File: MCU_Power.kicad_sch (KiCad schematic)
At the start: 36 parts, among them U3 SPC5676RDK3MVU1R

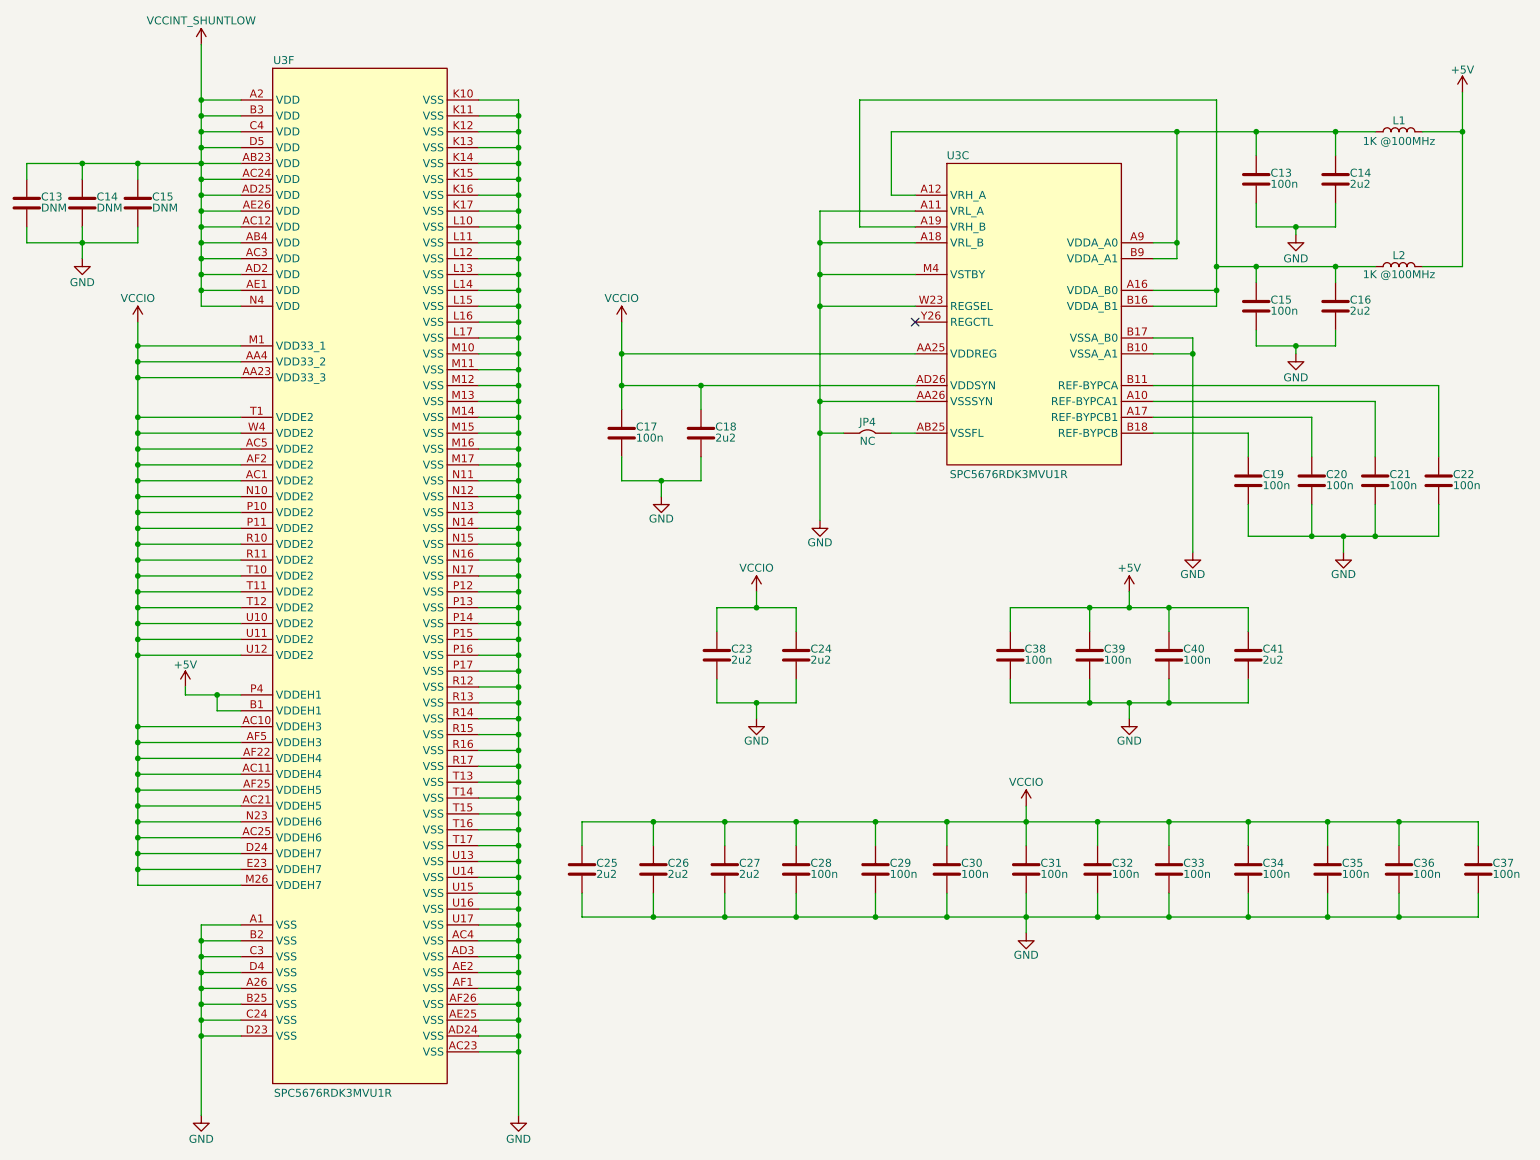
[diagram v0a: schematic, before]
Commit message: draft updated, schematic draft done, pcb issues with size of board and fitting all parts on
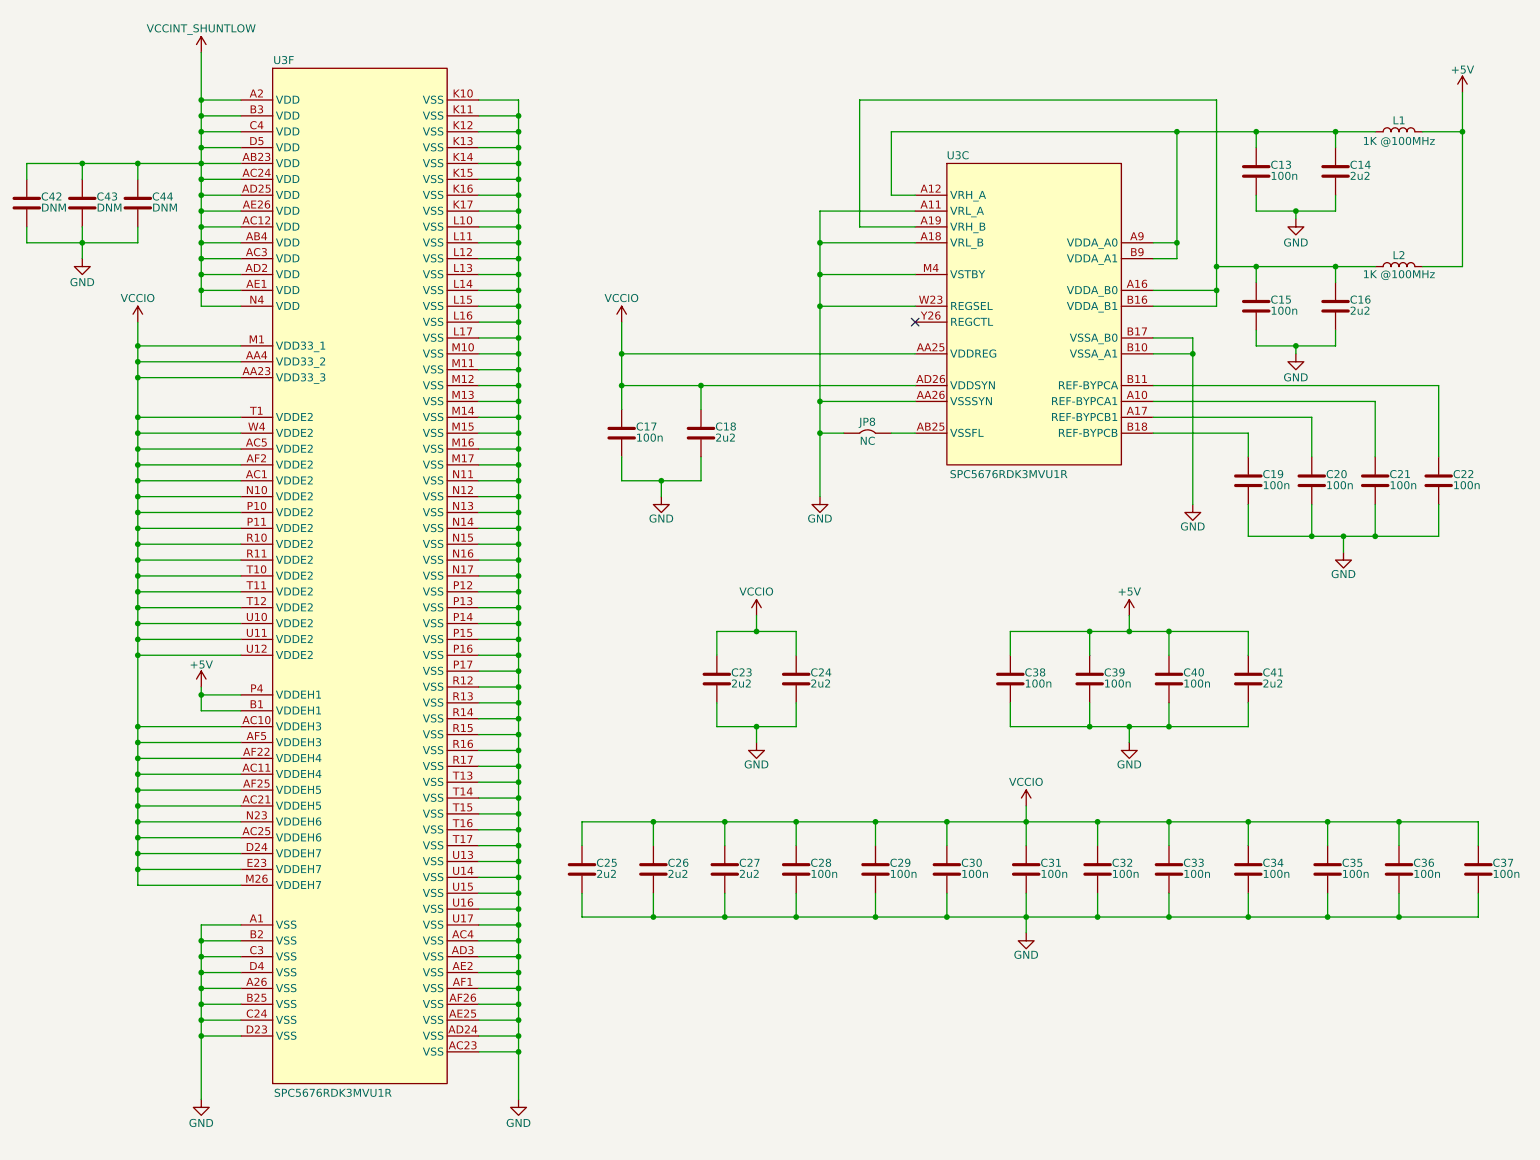
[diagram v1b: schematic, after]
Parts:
- renumbered C13 to C42, C14 to C43, C15 to C44, JP4 to JP8
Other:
- moved on the sheet: C13, C14, C23, C24, C38, C39, C40, C41

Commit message: updated schematic after library re-organization
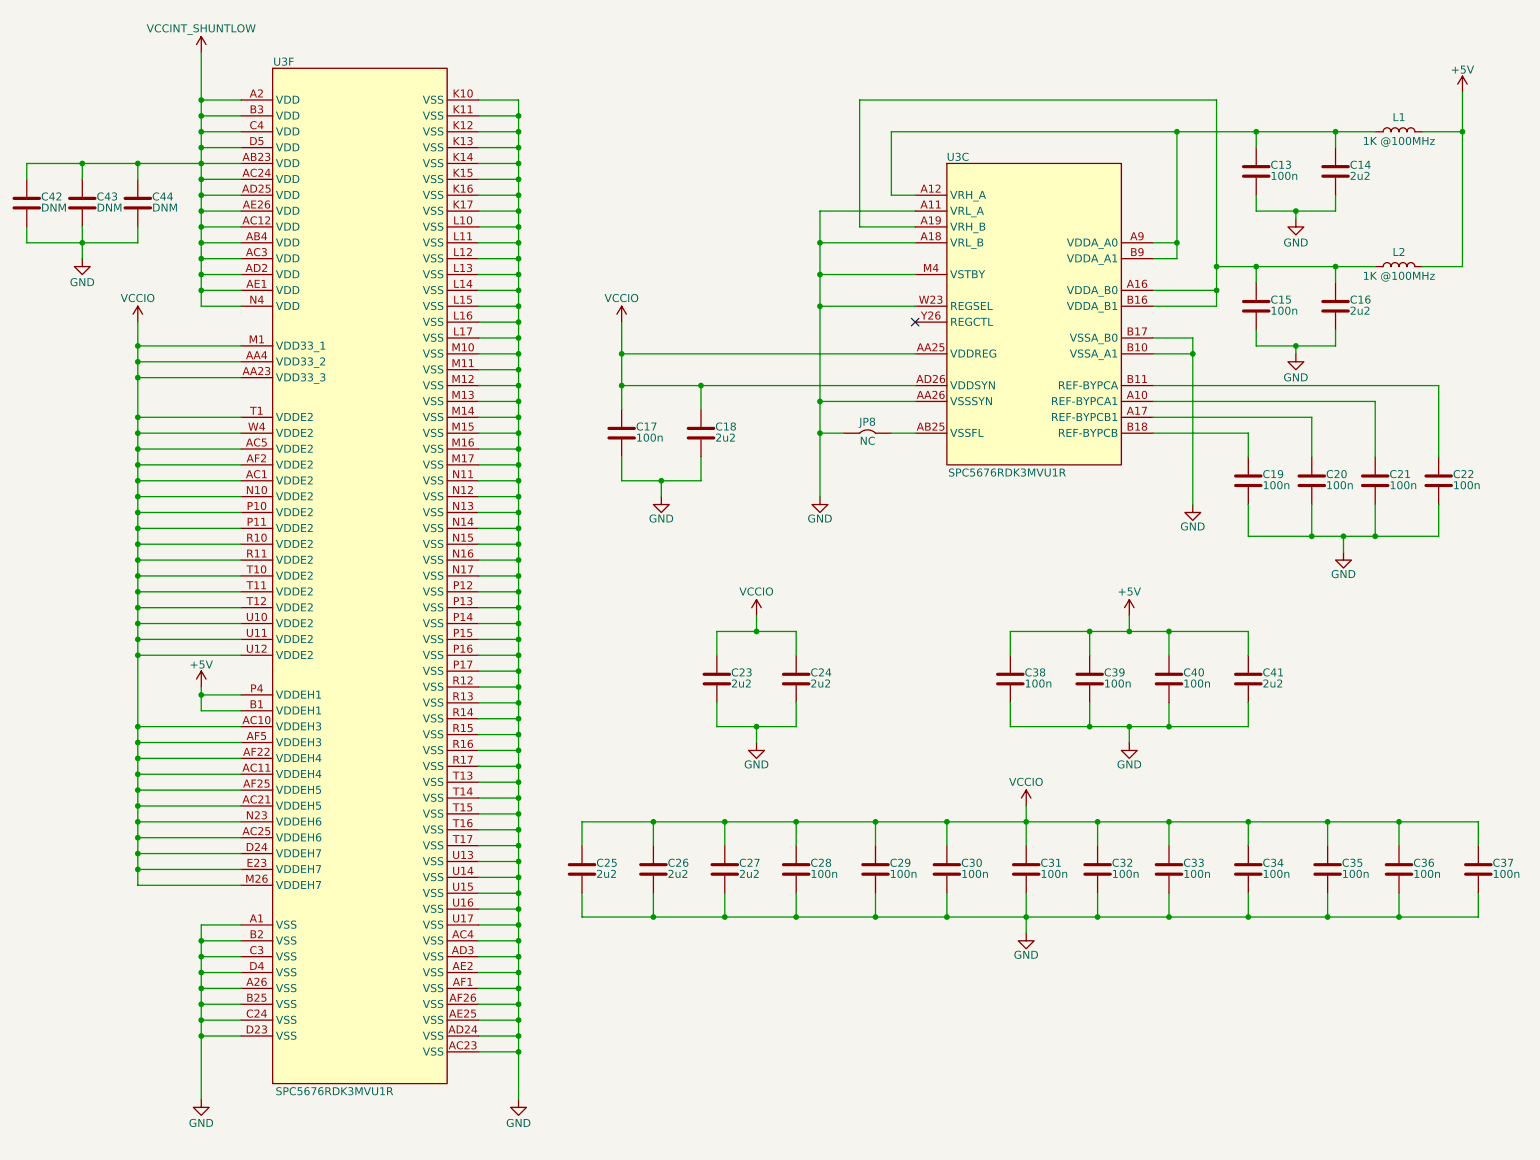
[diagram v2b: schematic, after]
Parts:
- removed JP8: ~, Jumper:SolderJumper-2_P1.3mm_Bridged2Bar_Pad1.0x1.5mm, symbol tutorial_2_library:Solder_Jumper_2_NC
- removed L1, L2: IND_1K_0603, Inductor_SMD:L_0603_1608Metric, symbol tutorial_2_library:IND_1K_100MHz_0603
- removed U3: SPC5676RDK3MVU1R, tutorial_2_library:BGA416C100P26X26_2700X2700X255N, symbol tutorial_2_library:SPC5676RDK3MVU1R
- added JP8: ~, Jumper:SolderJumper-2_P1.3mm_Bridged2Bar_Pad1.0x1.5mm, symbol NAE_Connectors:Solder_Jumper_2_NC
- added L1, L2: IND_1K_0603, Inductor_SMD:L_0603_1608Metric, symbol NAE_Inductors:IND_1K_100MHz_0603
- added U3: SPC5676RDK3MVU1R, tutorial_2_library:BGA416C100P26X26_2700X2700X255N, symbol NAE_Integrated_Circuits:SPC5676RDK3MVU1R
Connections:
- net +5V: now also L1.2, L2.2, U3.B1 (VDDEH1), U3.P4 (VDDEH1)
- net GND: now also JP8.2, U3.A1 (VSS), U3.A11 (VRL_A), U3.A18 (VRL_B), U3.A26 (VSS), U3.AA26 (VSSSYN), U3.AC23 (VSS), U3.AC4 (VSS), U3.AD24 (VSS), U3.AD3 (VSS), U3.AE2 (VSS), U3.AE25 (VSS), U3.AF1 (VSS), U3.AF26 (VSS), U3.B10 (VSSA_A1), U3.B17 (VSSA_B0), U3.B2 (VSS), U3.B25 (VSS), U3.C24 (VSS), U3.C3 (VSS), U3.D23 (VSS), U3.D4 (VSS), U3.K10 (VSS), U3.K11 (VSS), U3.K12 (VSS), U3.K13 (VSS), U3.K14 (VSS), U3.K15 (VSS), U3.K16 (VSS), U3.K17 (VSS), U3.L10 (VSS), U3.L11 (VSS), U3.L12 (VSS), U3.L13 (VSS), U3.L14 (VSS), U3.L15 (VSS), U3.L16 (VSS), U3.L17 (VSS), U3.M10 (VSS), U3.M11 (VSS), U3.M12 (VSS), U3.M13 (VSS), U3.M14 (VSS), U3.M15 (VSS), U3.M16 (VSS), U3.M17 (VSS), U3.M4 (VSTBY), U3.N11 (VSS), U3.N12 (VSS), U3.N13 (VSS), U3.N14 (VSS), U3.N15 (VSS), U3.N16 (VSS), U3.N17 (VSS), U3.P12 (VSS), U3.P13 (VSS), U3.P14 (VSS), U3.P15 (VSS), U3.P16 (VSS), U3.P17 (VSS), U3.R12 (VSS), U3.R13 (VSS), U3.R14 (VSS), U3.R15 (VSS), U3.R16 (VSS), U3.R17 (VSS), U3.T13 (VSS), U3.T14 (VSS), U3.T15 (VSS), U3.T16 (VSS), U3.T17 (VSS), U3.U13 (VSS), U3.U14 (VSS), U3.U15 (VSS), U3.U16 (VSS), U3.U17 (VSS), U3.W23 (REGSEL)
- net VCCINT_SHUNTLOW: now also U3.A2 (VDD), U3.AB23 (VDD), U3.AB4 (VDD), U3.AC12 (VDD), U3.AC24 (VDD), U3.AC3 (VDD), U3.AD2 (VDD), U3.AD25 (VDD), U3.AE1 (VDD), U3.AE26 (VDD), U3.B3 (VDD), U3.C4 (VDD), U3.D5 (VDD), U3.N4 (VDD)
- net VCCIO: now also U3.AA23 (VDD33_3), U3.AA25 (VDDREG), U3.AA4 (VDD33_2), U3.AC1 (VDDE2), U3.AC10 (VDDEH3), U3.AC11 (VDDEH4), U3.AC21 (VDDEH5), U3.AC25 (VDDEH6), U3.AC5 (VDDE2), U3.AD26 (VDDSYN), U3.AF2 (VDDE2), U3.AF22 (VDDEH4), U3.AF25 (VDDEH5), U3.AF5 (VDDEH3), U3.D24 (VDDEH7), U3.E23 (VDDEH7), U3.M1 (VDD33_1), U3.M26 (VDDEH7), U3.N10 (VDDE2), U3.N23 (VDDEH6), U3.P10 (VDDE2), U3.P11 (VDDE2), U3.R10 (VDDE2), U3.R11 (VDDE2), U3.T1 (VDDE2), U3.T10 (VDDE2), U3.T11 (VDDE2), U3.T12 (VDDE2), U3.U10 (VDDE2), U3.U11 (VDDE2), U3.U12 (VDDE2), U3.W4 (VDDE2)
- net at C20.2: now also U3.A17 (REF-BYPCB1)
- net at C15.2, C16.2: now also L2.1, U3.A16 (VDDA_B0), U3.A19 (VRH_B), U3.B16 (VDDA_B1)
- net at C21.2: now also U3.A10 (REF-BYPCA1)
- net at C13.2, C14.2: now also L1.1, U3.A12 (VRH_A), U3.A9 (VDDA_A0), U3.B9 (VDDA_A1)
- net at C22.2: now also U3.B11 (REF-BYPCA)
- net at C19.2: now also U3.B18 (REF-BYPCB)
- new net: JP8.1, U3.AB25 (VSSFL)
